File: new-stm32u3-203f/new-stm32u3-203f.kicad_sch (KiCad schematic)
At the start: 57 parts, among them J1 DM3CS-SF, J2 SJ-3524-SMT, J3 12401826E412A, SW1 SW_SPDT, U1 STM32U385RGT6Q, U2 TLV320DAC3203IRGER, U3 TCPP01-M12, U4 LD39050PU33R, U5 TLV62569DBVR, X1 32.768kHz

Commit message: did the power pins
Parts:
- added C32: 4.7u, symbol Device:C
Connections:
- net AVDD is gone; now on net +3V3: C1.2, C2.2, C21.2, C22.2, C23.2, C24.2, C25.2, C5.2, C6.2, U1.1 (VBAT), U1.13 (VDDA), U1.19 (VDD), U1.29 (VDDSMPS), U1.33 (VDD), U1.64 (VDD)
- net GNDREF: now also C32.2
- net V11: now also C32.1
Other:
- added sheet USB (untitled.kicad_sch)

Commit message: moved sections to their own sheets. much cleaner now :)
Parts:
- removed C1, C14, C16, C18, C26, C28, C30: 1u, symbol Device:C
- removed C10, C11: 6.8pF, symbol Device:C
- removed C12, C13: 47u, symbol Device:C
- removed C15, C17: 0.1u, symbol Device:C
- removed C19, C3, C4: 2.2u, symbol Device:C
- removed C2, C20, C22, C23, C24, C25, C27, C29, C6, C7, C9: 100n, symbol Device:C
- removed C21, C31, C5, C8: 10u, symbol Device:C
- removed C32: 4.7u, symbol Device:C
- removed CR1: USBLC6-2SC6, SOT23-6L_STM, symbol 2026-01-23_08-11-04:USBLC6-2SC6
- removed CR2: ESDA25P35-1U1M, QFN1610_STM, symbol 2026-01-24_13-06-26:ESDA25P35-1U1M
- removed CR3: BAT54KFILM, SOD-523_STM, symbol 2026-01-26_03-59-16:BAT54KFILM
- removed J1: DM3CS-SF, DM3CS-SF_HIR, symbol 2026-01-24_09-53-21:DM3CS-SF
- removed J2: SJ-3524-SMT, SJ-3524-SMT:CUI_SJ-3524-SMT, symbol SJ-3524-SMT:SJ-3524-SMT
- removed J3: 12401826E412A, 12401826_AMP, symbol 2026-01-23_08-02-34:12401826E412A
- removed L1, L2: 2.2uH, symbol Device:L
- removed MOSFET1: STL11N3LLH6, POWERFLAT-3p3X3p3_STM, symbol 2026-01-26_04-02-48:STL11N3LLH6
- removed R1: 10k, symbol Device:R
- removed R2, R5: 0R, symbol Device:R
- removed R3: 2K4, symbol Device:R
- removed R4: 10K, symbol Device:R
- removed R6, R7: 200k, symbol Device:R
- removed SW1: SW_SPDT, symbol Switch:SW_SPDT
- removed TP1: 3V3, symbol Connector:TestPoint
- removed TP2: 5V, symbol Connector:TestPoint
- removed TP3: 1V8, symbol Connector:TestPoint
- removed U1: STM32U385RGT6Q, LQFP64_STM, symbol 2026-01-21_08-27-02:STM32U385RGT6Q
- removed U2: TLV320DAC3203IRGER, RGE24_2P7X2P7_TEX, symbol 2026-01-22_06-52-15:TLV320DAC3203IRGER
- removed U3: TCPP01-M12, QFN12_TCPP01-M12_STM, symbol 2026-01-26_03-34-42:TCPP01-M12
- removed U4: LD39050PU33R, DFN6_3X3_STM, symbol 2026-01-26_04-25-52:LD39050PU33R
- removed U5: TLV62569DBVR, DBV0005A_N, symbol 2026-01-26_07-03-52:TLV62569DBVR
- removed X1: 32.768kHz, symbol Device:Crystal
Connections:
- no-connect marks 16 -> 0
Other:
- added sheet BASIC_IO (new-stm32u3-203f-BASC_IO.kicad_sch)
- added sheet MCU_IO (new-stm32u3-203d-MCU_IO.kicad_sch)
- added sheet MCU_PWR (new-stm32u3-203f-MCU_PWR.kicad_sch)
- added sheet POWER (new-stm32u3-203f-POWER.kicad_sch)
- added sheet SD_DAC (new-stm32u3-203f-SD_DAC.kicad_sch)
- sheet USB: file untitled.kicad_sch -> new-stm32u3-203f-USB.kicad_sch

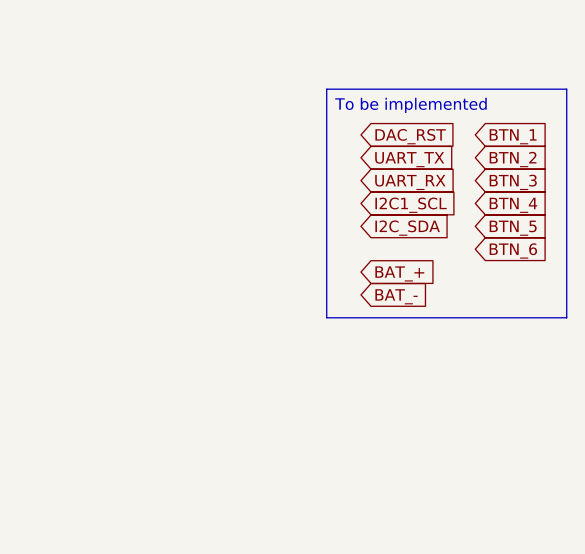
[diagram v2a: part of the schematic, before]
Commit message: added battery charging circuit
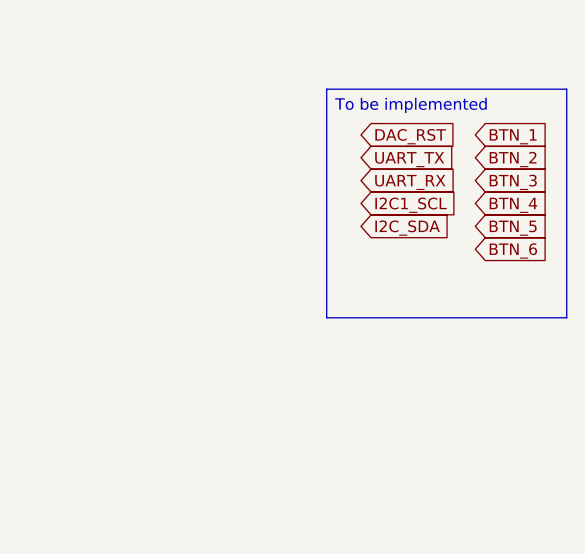
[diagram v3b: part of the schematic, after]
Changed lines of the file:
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@@
-		)
-	)
-	(global_label "BAT_-"
-		(shape input)
-		(at 213.36 72.39 0)
-		(fields_autoplaced yes)
-		(effects
-			(font
-				(size 1.27 1.27)
-			)
-			(justify left)
-		)
-		(property "Intersheetrefs" "${INTERSHEET_REFS}"
-			(at 222.2114 72.39 0)
-			(effects
-				(font
-					(size 1.27 1.27)
-				)
-				(justify left)
-				(hide yes)
-			)
 		)
 	)
@@
 			(effects
 				(font
-					(size 1.27 1.27)
-				)
-				(justify left)
-				(hide yes)
-			)
-		)
-	)
-	(global_label "BAT_+"
-		(shape input)
-		(at 213.36 69.85 0)
-		(fields_autoplaced yes)
-		(effects
-			(font
-				(size 1.27 1.27)
-			)
-			(justify left)
-		)
-		(property "Intersheetrefs" "${INTERSHEET_REFS}"
-			(at 222.2114 69.85 0)
-			(effects
-				(font

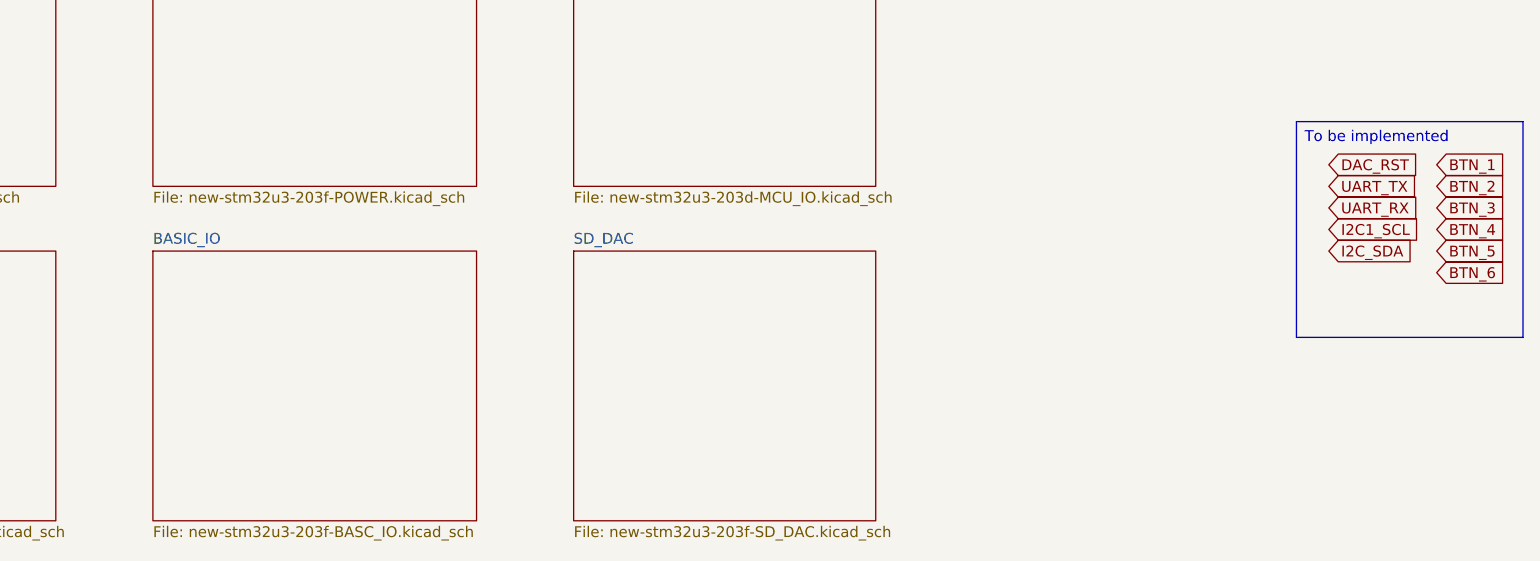
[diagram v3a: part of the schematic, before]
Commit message: added buttons, added uart, added display.
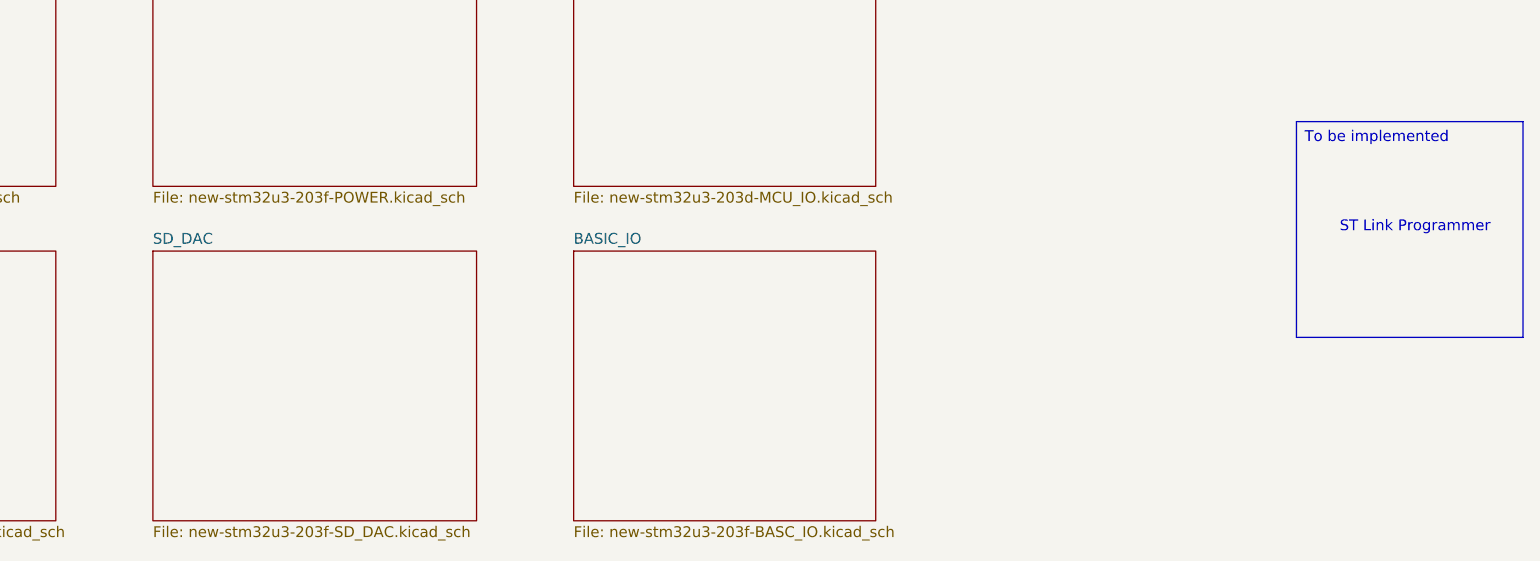
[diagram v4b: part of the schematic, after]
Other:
- note added: "ST Link Programmer"
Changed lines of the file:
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@@
 	(generator_version "9.0")
 	(paper "A4")
+	(text "ST Link Programmer\n"
+		(exclude_from_sim no)
+		(at 223.52 61.976 0)
+		(effects
+			(font
+				(size 1.27 1.27)
+			)
+		)
+	)
 	(text_box "To be implemented"
 		(exclude_from_sim no)
@@
 		)
 	)
-	(global_label "DAC_RST"
-		(shape input)
-		(at 213.36 54.61 0)
-		(fields_autoplaced yes)
-		(effects
-			(font
-				(size 1.27 1.27)
-			)
-			(justify left)
-		)
-		(property "Intersheetrefs" "${INTERSHEET_REFS}"
-			(at 224.3885 54.61 0)
-			(effects
-				(font
-					(size 1.27 1.27)
-				)
-				(justify left)
-				(hide yes)
-			)
-		)
-	)
-	(global_label "BTN_4"
-		(shape input)
-		(at 226.06 62.23 0)
-		(fields_autoplaced yes)
-		(effects
-			(font
-				(size 1.27 1.27)
-			)
-			(justify left)
-		)
-		(property "Intersheetrefs" "${INTERSHEET_REFS}"
-			(at 234.7904 62.23 0)
-			(effects
-				(font
-					(size 1.27 1.27)
-				)
-				(justify left)
-				(hide yes)
-			)
-		)
-	)
-	(global_label "I2C_SDA"
-		(shape input)
-		(at 213.36 64.77 0)
-		(fields_autoplaced yes)
-		(effects
-			(font
-				(size 1.27 1.27)
-			)
-			(justify left)
-		)
-		(property "Intersheetrefs" "${INTERSHEET_REFS}"
-			(at 223.9652 64.77 0)
-			(effects
-				(font
-					(size 1.27 1.27)
-				)
-				(justify left)
-				(hide yes)
-			)
-		)
-	)
-	(global_label "BTN_6"
-		(shape input)
-		(at 226.06 67.31 0)
-		(fields_autoplaced yes)
-		(effects
-			(font
-				(size 1.27 1.27)
-			)
-			(justify left)
-		)
-		(property "Intersheetrefs" "${INTERSHEET_REFS}"
-			(at 234.7904 67.31 0)
-			(effects
-				(font
-					(size 1.27 1.27)
-				)
-				(justify left)
-				(hide yes)
-			)
-		)
-	)
-	(global_label "BTN_1"
-		(shape input)
-		(at 226.06 54.61 0)
-		(fields_autoplaced yes)
-		(effects
-			(font
-				(size 1.27 1.27)
-			)
-			(justify left)
-		)
-		(property "Intersheetrefs" "${INTERSHEET_REFS}"
-			(at 234.7904 54.61 0)
-			(effects
-				(font
-					(size 1.27 1.27)
-				)
-				(justify left)
-				(hide yes)
-			)
-		)
-	)
-	(global_label "UART_TX"
-		(shape input)
-		(at 213.36 57.15 0)
-		(fields_autoplaced yes)
-		(effects
-			(font
-				(size 1.27 1.27)
-			)
-			(justify left)
-		)
-		(property "Intersheetrefs" "${INTERSHEET_REFS}"
-			(at 224.1466 57.15 0)
-			(effects
-				(font
-					(size 1.27 1.27)
-				)
-				(justify left)
-				(hide yes)
-			)
-		)
-	)
-	(global_label "BTN_5"
-		(shape input)
-		(at 226.06 64.77 0)
-		(fields_autoplaced yes)
-		(effects
-			(font
-				(size 1.27 1.27)
-			)
-			(justify left)
-		)
-		(property "Intersheetrefs" "${INTERSHEET_REFS}"
-			(at 234.7904 64.77 0)
-			(effects
-				(font
-					(size 1.27 1.27)
-				)
-				(justify left)
-				(hide yes)
-			)
-		)
-	)
-	(global_label "UART_RX"
-		(shape input)
-		(at 213.36 59.69 0)
-		(fields_autoplaced yes)
-		(effects
-			(font
-				(size 1.27 1.27)
-			)
-			(justify left)
-		)
-		(property "Intersheetrefs" "${INTERSHEET_REFS}"
-			(at 224.449 59.69 0)
-			(effects
-				(font
-					(size 1.27 1.27)
-				)
-				(justify left)
-				(hide yes)
-			)
-		)
-	)
-	(global_label "BTN_2"
-		(shape input)
-		(at 226.06 57.15 0)
-		(fields_autoplaced yes)
-		(effects
-			(font
-				(size 1.27 1.27)
-			)
-			(justify left)
-		)
-		(property "Intersheetrefs" "${INTERSHEET_REFS}"
-			(at 234.7904 57.15 0)
-			(effects
-				(font
-					(size 1.27 1.27)
-				)
-				(justify left)
-				(hide yes)
-			)
-		)
-	)
-	(global_label "BTN_3"
-		(shape input)
-		(at 226.06 59.69 0)
-		(fields_autoplaced yes)
-		(effects
-			(font
-				(size 1.27 1.27)
-			)
-			(justify left)
-		)
-		(property "Intersheetrefs" "${INTERSHEET_REFS}"
-			(at 234.7904 59.69 0)
-			(effects
-				(font
-					(size 1.27 1.27)
-				)
-				(justify left)
-				(hide yes)
-			)
-		)
-	)
-	(global_label "I2C1_SCL"
-		(shape input)
-		(at 213.36 62.23 0)
-		(fields_autoplaced yes)
-		(effects
-			(font
-				(size 1.27 1.27)
-			)
-			(justify left)
-		)
-		(property "Intersheetrefs" "${INTERSHEET_REFS}"
-			(at 225.1142 62.23 0)
-			(effects
-				(font
-					(size 1.27 1.27)
-				)
-				(justify left)
-				(hide yes)
-			)
-		)
-	)
 	(sheet
 		(at 124.46 25.4)
@@
 	)
 	(sheet
+		(at 74.93 64.77)
+		(size 38.1 31.75)
+		(exclude_from_sim no)
+		(in_bom yes)
+		(on_board yes)
+		(dnp no)
+		(fields_autoplaced yes)
+		(stroke
+			(width 0.1524)
+			(type solid)
+		)
+		(fill
+			(color 0 0 0 0.0000)
+		)
+		(property "Sheetname" "SD_DAC"
+			(at 74.93 64.0584 0)
+			(effects
+				(font
+					(size 1.27 1.27)
+				)
+				(justify left bottom)
+			)
+		)
+		(property "Sheetfile" "new-stm32u3-203f-SD_DAC.kicad_sch"
+			(at 74.93 97.1046 0)
+			(effects
+				(font
+					(size 1.27 1.27)
+				)
+				(justify left top)
+			)
+		)
+		(instances
+			(project "new-stm32u3-203f"
+				(path "/133609ce-1e1a-4c9a-bce3-37a0219dc965"
+					(page "6")
+				)
+			)
+		)
+	)
+	(sheet
 		(at 124.46 64.77)
 		(size 35.56 31.75)
@@
 			(color 0 0 0 0.0000)
 		)
-		(property "Sheetname" "SD_DAC"
+		(property "Sheetname" "BASIC_IO"
 			(at 124.46 64.0584 0)
 			(effects
@@
 			)
 		)
-		(property "Sheetfile" "new-stm32u3-203f-SD_DAC.kicad_sch"
+		(property "Sheetfile" "new-stm32u3-203f-BASC_IO.kicad_sch"
 			(at 124.46 97.1046 0)
 			(effects
 				(font
-					(size 1.27 1.27)
-				)
-				(justify left top)
-			)
-		)
-		(instances
-			(project "new-stm32u3-203f"
-				(path "/133609ce-1e1a-4c9a-bce3-37a0219dc965"
-					(page "6")
-				)
-			)
-		)
-	)
-	(sheet
-		(at 74.93 64.77)
-		(size 38.1 31.75)
-		(exclude_from_sim no)
-		(in_bom yes)
-		(on_board yes)
-		(dnp no)
-		(fields_autoplaced yes)
-		(stroke
-			(width 0.1524)
-			(type solid)
-		)
-		(fill
-			(color 0 0 0 0.0000)
-		)
-		(property "Sheetname" "BASIC_IO"
-			(at 74.93 64.0584 0)
-			(effects
-				(font
-					(size 1.27 1.27)
-				)
-				(justify left bottom)
-			)
-		)
-		(property "Sheetfile" "new-stm32u3-203f-BASC_IO.kicad_sch"
-			(at 74.93 97.1046 0)
-			(effects
-				(font

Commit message: finished the schematic, just need someone to review it :)
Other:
- note removed: "ST Link Programmer"
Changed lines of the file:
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@@
 	(generator_version "9.0")
 	(paper "A4")
-	(text "ST Link Programmer\n"
-		(exclude_from_sim no)
-		(at 223.52 61.976 0)
-		(effects
-			(font
-				(size 1.27 1.27)
-			)
-		)
-	)
-	(text_box "To be implemented"
-		(exclude_from_sim no)
-		(at 209.55 49.53 0)
-		(size 26.67 25.4)
-		(margins 0.9525 0.9525 0.9525 0.9525)
-		(stroke
-			(width 0)
-			(type solid)
-		)
-		(fill
-			(type none)
-		)
-		(effects
-			(font
-				(size 1.27 1.27)
-			)
-			(justify left top)
-		)
-	)
 	(sheet
 		(at 124.46 25.4)
